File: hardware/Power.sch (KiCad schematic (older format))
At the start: 17 parts, among them K11 G5V-2-DC12, U2 V7805-1000

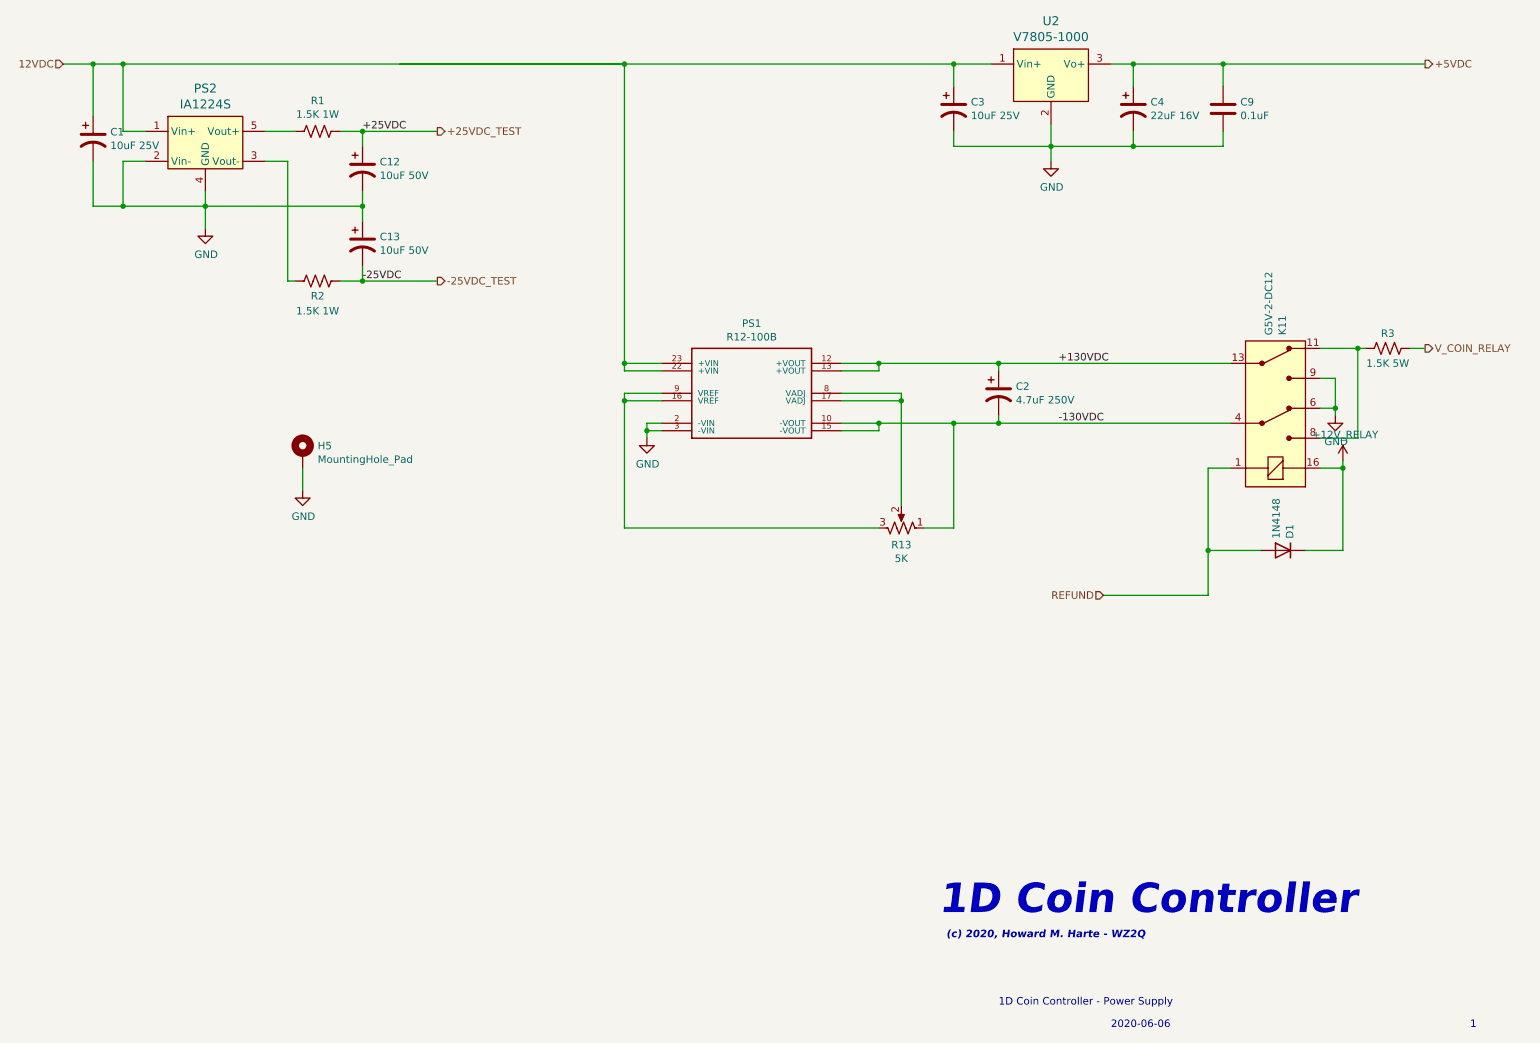
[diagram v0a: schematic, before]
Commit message: Issue 2 schmatic and Layout
Added polarity reversal detection to monitor answer supervision.
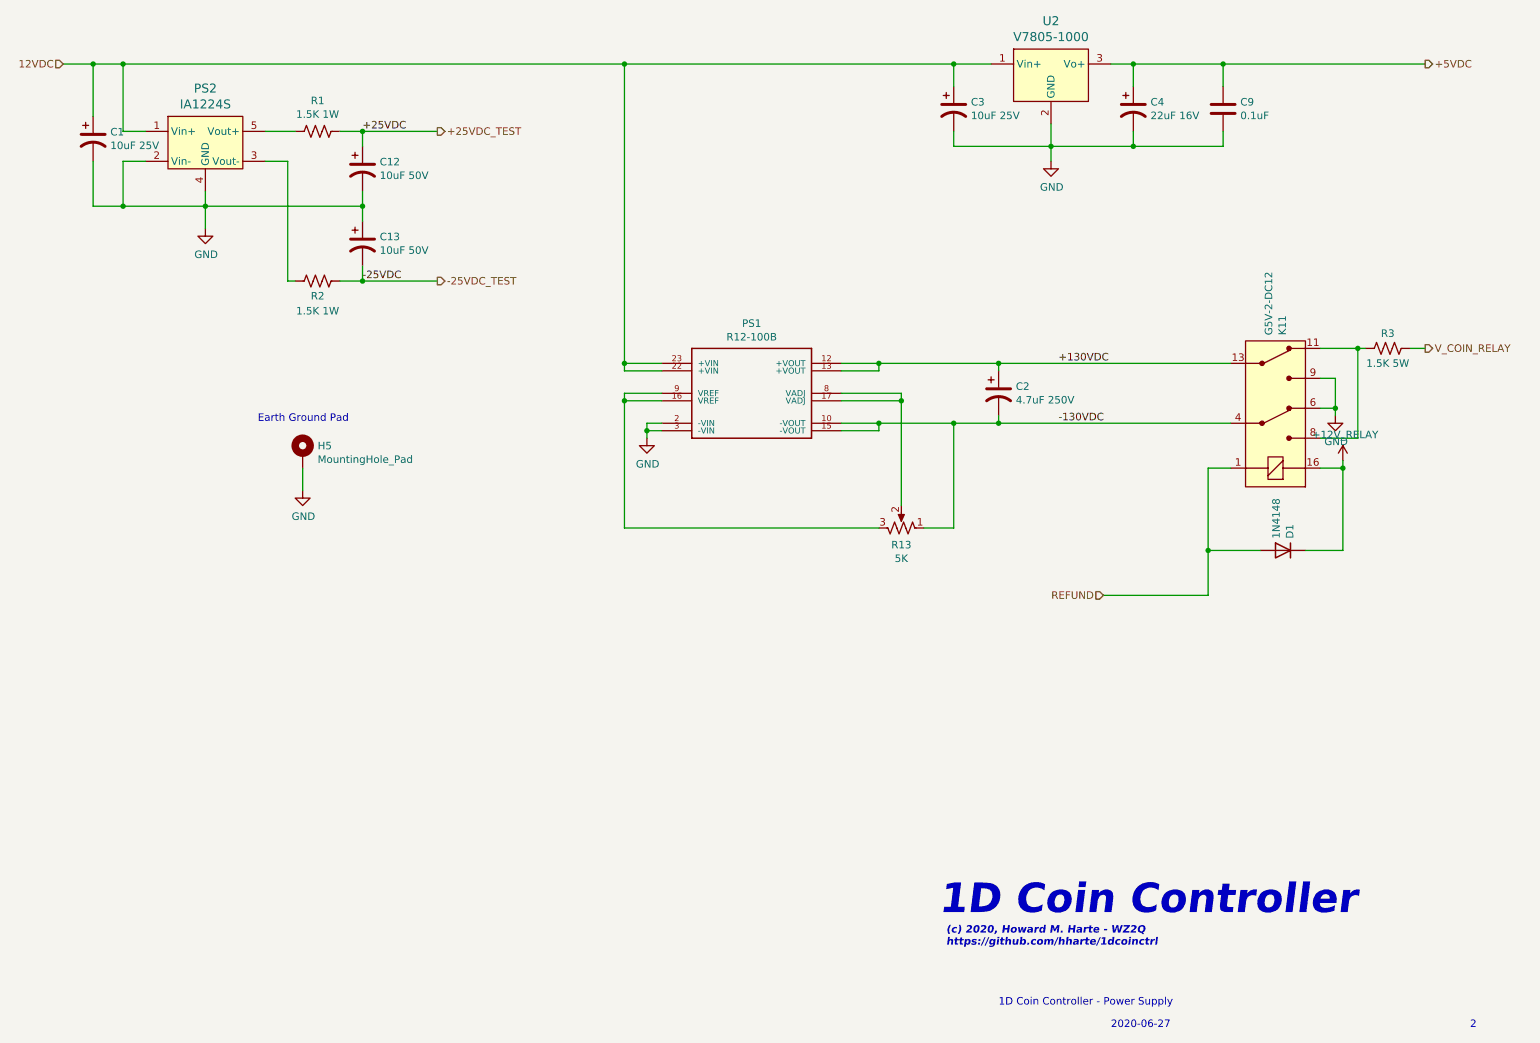
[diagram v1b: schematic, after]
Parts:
- C2: footprint Capacitor_THT:CP_Radial_D10.0mm_P5.00mm -> Capacitor_THT:CP_Radial_D8.0mm_P3.50mm
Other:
- note added: "(c) 2020, Howard M. Harte - WZ2Q\nhttps://github.com/hharte/1dcoinctrl"
- note added: "2"
- note added: "2020-06-27"
- note added: "Earth Ground Pad"
- note removed: "(c) 2020, Howard M. Harte - WZ2Q"
- note removed: "1"
- note removed: "2020-06-06"
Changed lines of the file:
@@
 F 0 "C2" H 7515 3446 50  0000 L CNN
 F 1 "4.7uF 250V" H 7515 3355 50  0000 L CNN
-F 2 "Capacitor_THT:CP_Radial_D10.0mm_P5.00mm" H 7400 3400 50  0001 C CNN
+F 2 "Capacitor_THT:CP_Radial_D8.0mm_P3.50mm" H 7400 3400 50  0001 C CNN
 F 3 "~" H 7400 3400 50  0001 C CNN
 	1    7400 3400
@@
 	4900 1200 7100 1200
 Wire Wire Line
-	3400 1200 4900 1200
-Wire Wire Line
 	8300 1200 8900 1200
 Wire Wire Line
@@
 Text Notes 7000 6900 0    197  Italic 39
 1D Coin Controller
-Text Notes 7050 7050 0    50   Italic 10
-(c) 2020, Howard M. Harte - WZ2Q
 Text Notes 10550 7650 0    50   ~ 0
-1
+2
 Text Notes 7400 7500 0    50   ~ 0
 1D Coin Controller - Power Supply
 Text Notes 8150 7650 0    50   ~ 0
-2020-06-06
+2020-06-27
+Text Notes 2450 3600 0    50   ~ 0
+Earth Ground Pad
+Text Notes 7050 7100 0    50   Italic 10
+(c) 2020, Howard M. Harte - WZ2Q\nhttps://github.com/hharte/1dcoinctrl
 $EndSCHEMATC
